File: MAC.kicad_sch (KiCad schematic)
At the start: 32 parts, among them J10 Conn_01x08_Male, U12 LM358, U13 LM358

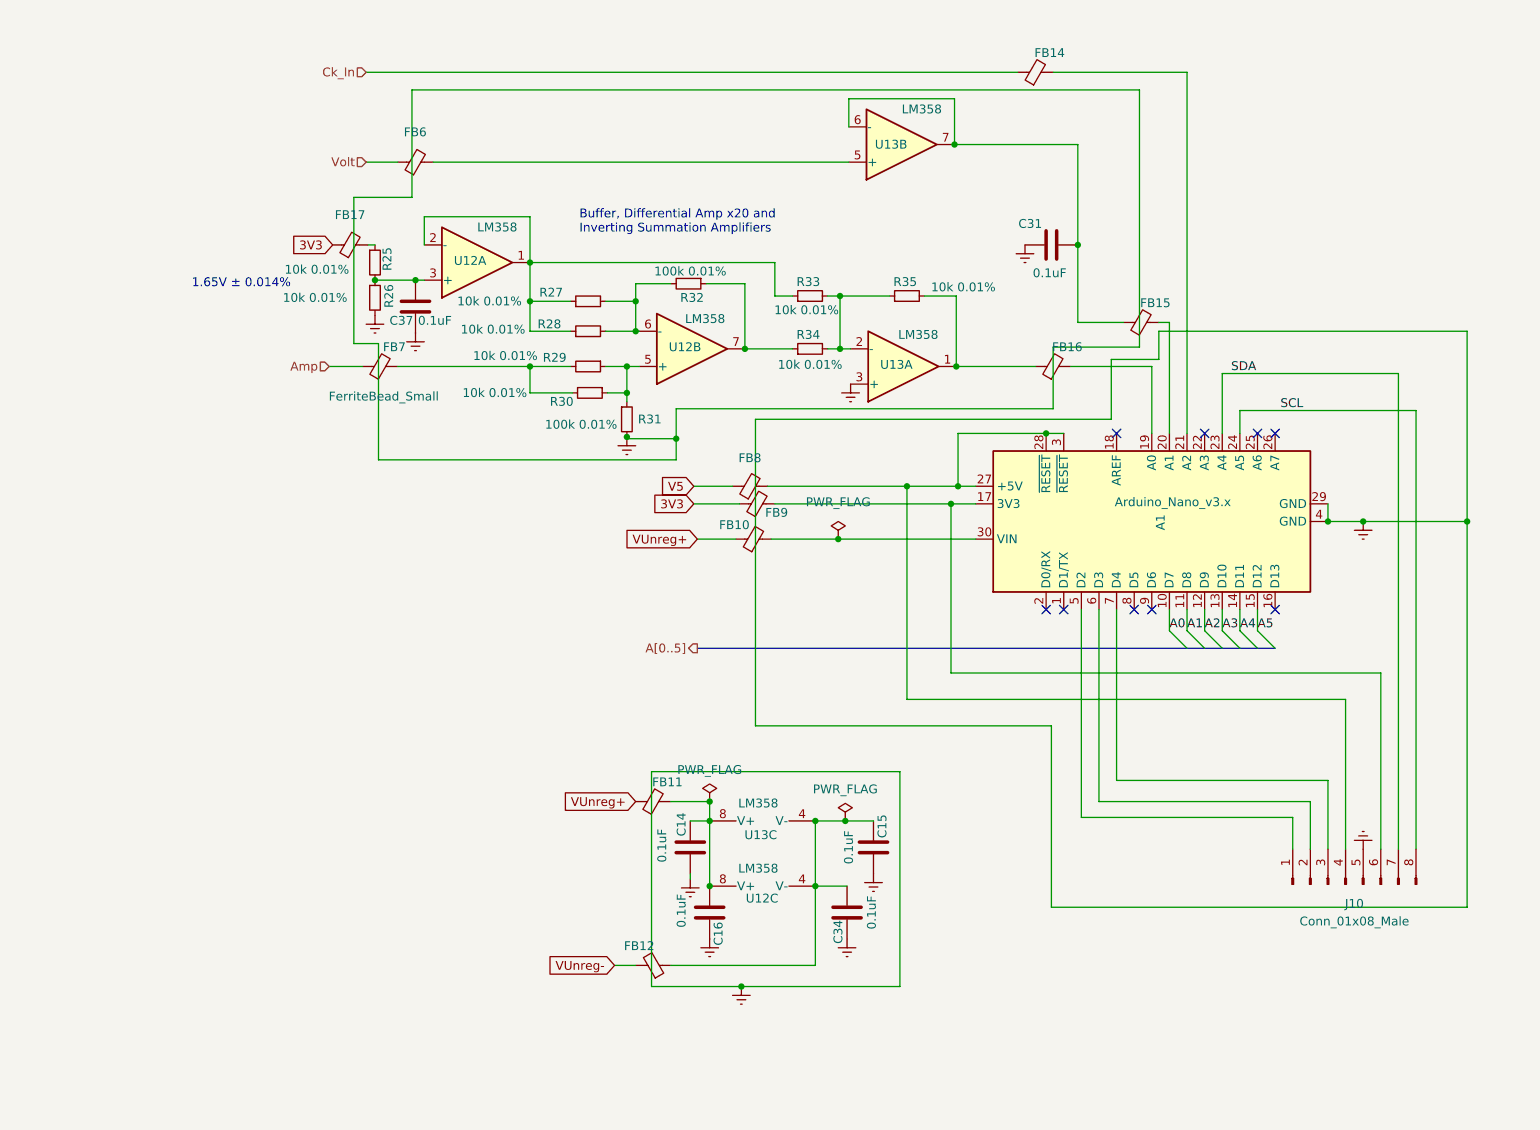
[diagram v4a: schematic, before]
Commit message: mux and opamp layouts completed and new ext conn to display
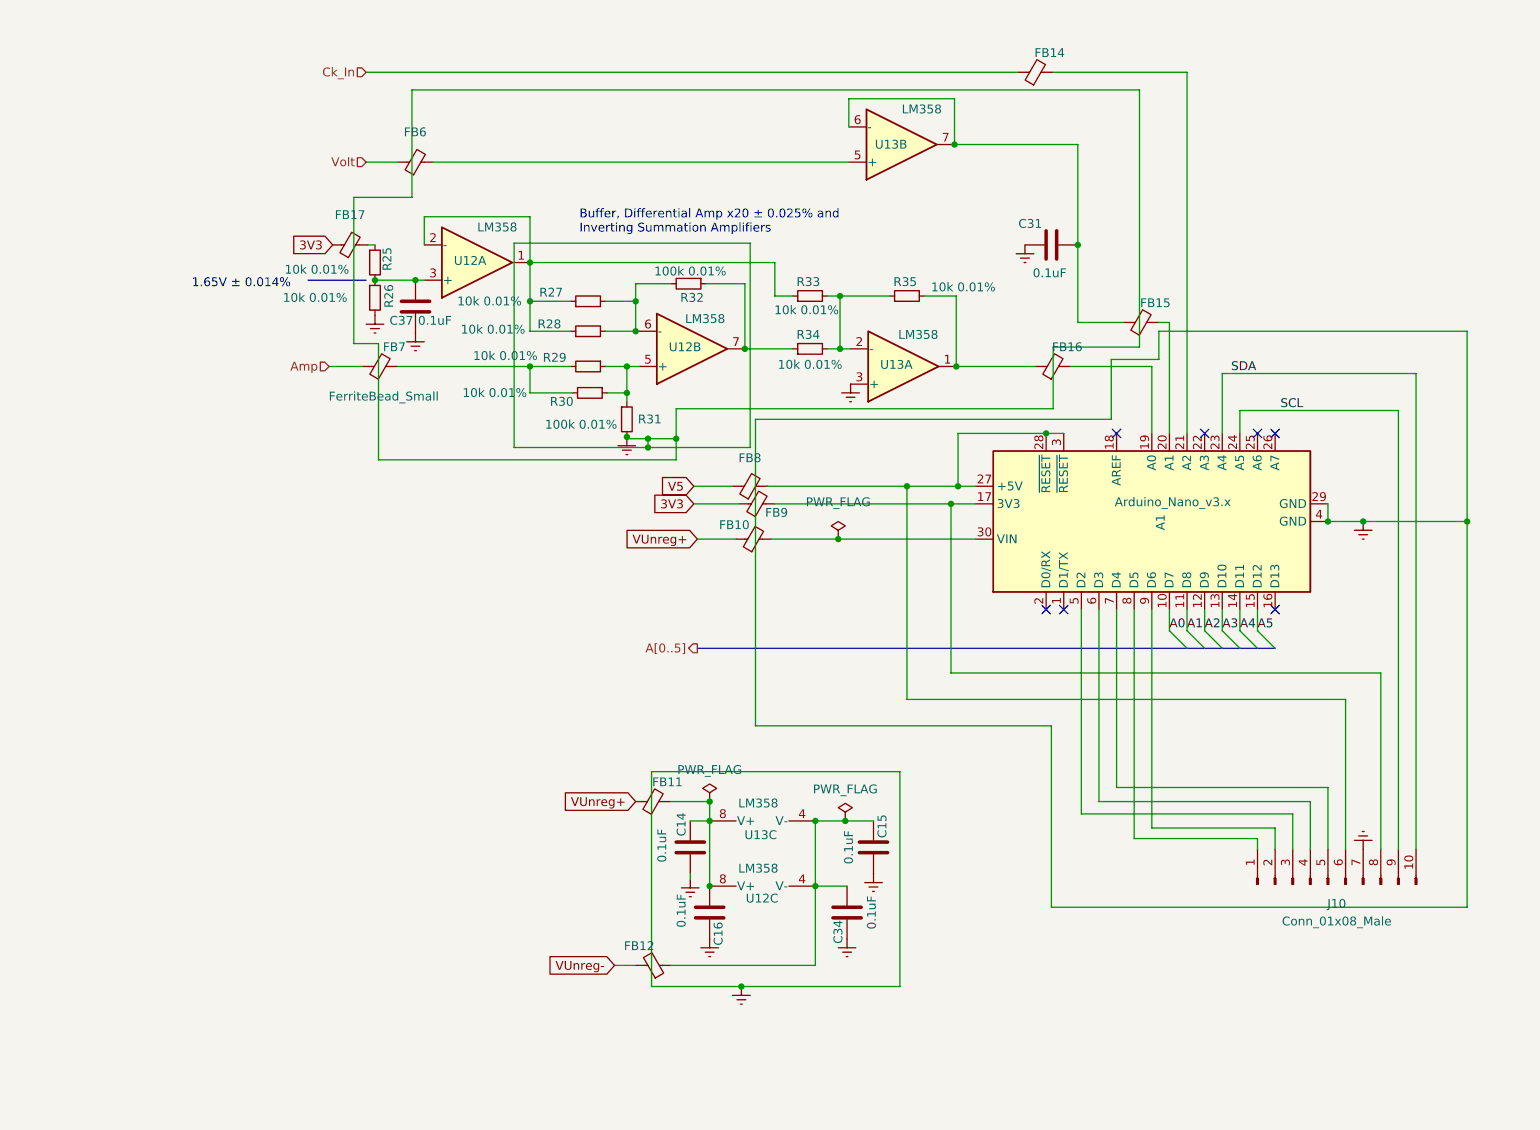
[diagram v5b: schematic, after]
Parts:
- J10: footprint Connector_PinHeader_2.54mm:PinHeader_1x08_P2.54mm_Vertical -> Connector_PinHeader_2.54mm:PinHeader_1x10_P2.54mm_Vertical; symbol Connector:Conn_01x08_Male -> Connector:Conn_01x10_Male
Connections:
- net GNDREF: now also J10.7 (Pin_7); no longer J10.5 (Pin_5)
- net SCL: now also J10.9 (Pin_9); no longer J10.8 (Pin_8)
- net SDA: now also J10.10 (Pin_10); no longer J10.7 (Pin_7)
- net at A1.17 (3V3), FB9.2: now also J10.8 (Pin_8); no longer J10.6 (Pin_6)
- net at J10.1 (Pin_1): now also A1.8 (D5); no longer A1.5 (D2)
- net at J10.2 (Pin_2): now also A1.9 (D6); no longer A1.6 (D3)
- net at J10.3 (Pin_3): now also A1.5 (D2); no longer A1.7 (D4)
- net at A1.27 (+5V), A1.28 (~{RESET}), A1.3 (~{RESET})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: now also J10.6 (Pin_6); no longer J10.4 (Pin_4)
- new net: A1.6 (D3), J10.4 (Pin_4)
- new net: A1.7 (D4), J10.5 (Pin_5)
- no-connect marks 9 -> 7
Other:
- note added: "Buffer, Differential Amp x20 ± 0.025% and Inverting Summation Amplifiers"
- note removed: "Buffer, Differential Amp x20 and Inverting Summation Amplifiers"
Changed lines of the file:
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@@
   (junction (at 120.142 138.684) (diameter 0) (color 0 0 0 0)
+  )
+  (junction (at 111.252 83.566) (diameter 0) (color 0 0 0 0)
+  )
+  (junction (at 111.252 84.836) (diameter 0) (color 0 0 0 0)
   )
   (junction (at 135.382 138.684) (diameter 0) (color 0 0 0 0)
@@
   (no_connect (at 171.196 108.204))
   (no_connect (at 168.656 108.204))
-  (no_connect (at 183.896 108.204))
-  (no_connect (at 181.356 108.204))
   (no_connect (at 201.676 82.804))
   (no_connect (at 191.516 82.804))
@@
     (stroke (width 0) (type default) (color 0 0 0 0))
   )
-  (wire (pts (xy 204.216 138.176) (xy 204.216 142.748))
+  (wire (pts (xy 204.216 137.668) (xy 204.216 142.748))
     (stroke (width 0) (type default) (color 0 0 0 0))
   )
@@
     (stroke (width 0) (type default) (color 0 0 0 0))
   )
+  (wire (pts (xy 91.948 55.372) (xy 91.948 84.836))
+    (stroke (width 0) (type default) (color 0 0 0 0))
+  )
   (wire (pts (xy 68.834 48.768) (xy 68.834 69.85))
     (stroke (width 0) (type default) (color 0 0 0 0))
@@
     (stroke (width 0) (type default) (color 0 0 0 0))
   )
+  (wire (pts (xy 181.356 141.224) (xy 199.136 141.224))
+    (stroke (width 0) (type default) (color 0 0 0 0))
+  )
+  (wire (pts (xy 181.356 108.204) (xy 181.356 141.224))
+    (stroke (width 0) (type default) (color 0 0 0 0))
+  )
   (wire (pts (xy 169.672 70.358) (xy 182.118 70.358))
     (stroke (width 0) (type default) (color 0 0 0 0))
@@
     (stroke (width 0) (type default) (color 0 0 0 0))
   )
+  (wire (pts (xy 91.948 55.372) (xy 125.984 55.372))
+    (stroke (width 0) (type default) (color 0 0 0 0))
+  )
   (wire (pts (xy 147.574 162.56) (xy 124.714 162.56))
     (stroke (width 0) (type default) (color 0 0 0 0))
@@
     (stroke (width 0) (type default) (color 0 0 0 0))
   )
+  (wire (pts (xy 201.676 142.748) (xy 201.676 139.7))
+    (stroke (width 0) (type default) (color 0 0 0 0))
+  )
   (wire (pts (xy 109.474 61.214) (xy 114.554 61.214))
     (stroke (width 0) (type default) (color 0 0 0 0))
@@
     (stroke (width 0) (type default) (color 0 0 0 0))
   )
+  (wire (pts (xy 219.456 79.502) (xy 219.456 142.748))
+    (stroke (width 0) (type default) (color 0 0 0 0))
+  )
   (wire (pts (xy 182.118 33.274) (xy 182.118 70.358))
     (stroke (width 0) (type default) (color 0 0 0 0))
   )
+  (wire (pts (xy 125.984 84.836) (xy 125.984 55.372))
+    (stroke (width 0) (type default) (color 0 0 0 0))
+  )
   (wire (pts (xy 68.834 48.768) (xy 77.216 48.768))
     (stroke (width 0) (type default) (color 0 0 0 0))
@@
     (stroke (width 0) (type default) (color 0 0 0 0))
   )
+  (wire (pts (xy 111.252 83.566) (xy 111.252 84.836))
+    (stroke (width 0) (type default) (color 0 0 0 0))
+  )
   (wire (pts (xy 77.724 60.706) (xy 78.994 60.706))
     (stroke (width 0) (type default) (color 0 0 0 0))
@@
     (stroke (width 0) (type default) (color 0 0 0 0))
   )
+  (wire (pts (xy 183.896 139.7) (xy 183.896 108.204))
+    (stroke (width 0) (type default) (color 0 0 0 0))
+  )
   (wire (pts (xy 115.316 86.614) (xy 115.316 83.566))
     (stroke (width 0) (type default) (color 0 0 0 0))
@@
     (stroke (width 0) (type default) (color 0 0 0 0))
   )
-  (wire (pts (xy 173.736 108.204) (xy 173.736 138.176))
+  (wire (pts (xy 173.736 108.204) (xy 173.736 137.668))
     (stroke (width 0) (type default) (color 0 0 0 0))
   )
@@
     (stroke (width 0) (type default) (color 0 0 0 0))
   )
-  (wire (pts (xy 196.596 79.502) (xy 221.996 79.502))
+  (wire (pts (xy 196.596 79.502) (xy 219.456 79.502))
     (stroke (width 0) (type default) (color 0 0 0 0))
   )
@@
     (stroke (width 0) (type default) (color 0 0 0 0))
   )
-  (wire (pts (xy 221.996 79.502) (xy 221.996 142.748))
-    (stroke (width 0) (type default) (color 0 0 0 0))
-  )
   (wire (pts (xy 117.856 92.964) (xy 124.46 92.964))
     (stroke (width 0) (type default) (color 0 0 0 0))
   )
-  (wire (pts (xy 173.736 138.176) (xy 204.216 138.176))
+  (wire (pts (xy 173.736 137.668) (xy 204.216 137.668))
     (stroke (width 0) (type default) (color 0 0 0 0))
   )
@@
     (stroke (width 0) (type default) (color 0 0 0 0))
   )
-  (wire (pts (xy 178.816 132.842) (xy 209.296 132.842))
+  (wire (pts (xy 178.816 133.858) (xy 209.296 133.858))
     (stroke (width 0) (type default) (color 0 0 0 0))
   )
@@
     (stroke (width 0) (type default) (color 0 0 0 0))
   )
+  (wire (pts (xy 91.948 84.836) (xy 111.252 84.836))
+    (stroke (width 0) (type default) (color 0 0 0 0))
+  )
   (wire (pts (xy 72.39 69.85) (xy 68.834 69.85))
     (stroke (width 0) (type default) (color 0 0 0 0))
@@
     (stroke (width 0) (type default) (color 0 0 0 0))
   )
-  (wire (pts (xy 108.204 83.566) (xy 115.316 83.566))
+  (wire (pts (xy 108.204 83.566) (xy 111.252 83.566))
     (stroke (width 0) (type default) (color 0 0 0 0))
   )
@@
     (stroke (width 0) (type default) (color 0 0 0 0))
   )
+  (wire (pts (xy 111.252 83.566) (xy 115.316 83.566))
+    (stroke (width 0) (type default) (color 0 0 0 0))
+  )
   (wire (pts (xy 140.208 34.544) (xy 155.448 34.544))
     (stroke (width 0) (type default) (color 0 0 0 0))
@@
     (stroke (width 0) (type default) (color 0 0 0 0))
   )
-  (wire (pts (xy 219.456 74.168) (xy 194.056 74.168))
+  (wire (pts (xy 201.676 139.7) (xy 183.896 139.7))
+    (stroke (width 0) (type default) (color 0 0 0 0))
+  )
+  (wire (pts (xy 194.056 74.168) (xy 221.996 74.168))
     (stroke (width 0) (type default) (color 0 0 0 0))
   )
@@
     (stroke (width 0) (type default) (color 0 0 0 0))
   )
+  (wire (pts (xy 221.996 74.168) (xy 221.996 142.748))
+    (stroke (width 0) (type default) (color 0 0 0 0))
+  )
   (wire (pts (xy 135.382 138.684) (xy 139.7 138.684))
     (stroke (width 0) (type default) (color 0 0 0 0))
@@
     (stroke (width 0) (type default) (color 0 0 0 0))
   )
-  (wire (pts (xy 219.456 74.168) (xy 219.456 142.748))
-    (stroke (width 0) (type default) (color 0 0 0 0))
-  )
   (wire (pts (xy 137.16 62.992) (xy 138.938 62.992))
     (stroke (width 0) (type default) (color 0 0 0 0))
@@
     (stroke (width 0) (type default) (color 0 0 0 0))
   )
-  (wire (pts (xy 178.816 108.204) (xy 178.816 132.842))
+  (wire (pts (xy 178.816 108.204) (xy 178.816 133.858))
     (stroke (width 0) (type default) (color 0 0 0 0))
   )
@@
     (stroke (width 0) (type default) (color 0 0 0 0))
   )
+  (wire (pts (xy 199.136 141.224) (xy 199.136 142.748))
+    (stroke (width 0) (type default) (color 0 0 0 0))
+  )
   (wire (pts (xy 120.142 135.89) (xy 120.142 138.684))
     (stroke (width 0) (type default) (color 0 0 0 0))
   )
+  (wire (pts (xy 111.252 84.836) (xy 125.984 84.836))
+    (stroke (width 0) (type default) (color 0 0 0 0))
+  )
   (bus (pts (xy 199.136 113.792) (xy 201.676 113.792))
     (stroke (width 0) (type default) (color 0 0 0 0))
@@
     (stroke (width 0) (type default) (color 0 0 0 0))
   )
+  (polyline (pts (xy 62.23 60.706) (xy 70.612 60.706))
+    (stroke (width 0) (type default) (color 0 0 0 0))
+  )
   (wire (pts (xy 129.54 58.166) (xy 94.234 58.166))
     (stroke (width 0) (type default) (color 0 0 0 0))
@@
     (stroke (width 0) (type default) (color 0 0 0 0))
   )
-  (wire (pts (xy 209.296 132.842) (xy 209.296 142.748))
+  (wire (pts (xy 209.296 133.858) (xy 209.296 142.748))
     (stroke (width 0) (type default) (color 0 0 0 0))
   )
@@
     (stroke (width 0) (type default) (color 0 0 0 0))
   )
-  (text "Buffer, Differential Amp x20 and\nInverting Summation Amplifiers"
+  (text "Buffer, Differential Amp x20 ± 0.025% and\nInverting Summation Amplifiers"
     (at 101.346 54.102 0)
     (effects (font (size 1.27 1.27)) (justify left bottom))
@@
     (pin "2")
   )
-  (symbol (lib_id "Connector:Conn_01x08_Male") (at 211.836 147.828 90) (unit 1)
+  (symbol (lib_id "Connector:Conn_01x10_Male") (at 209.296 147.828 90) (unit 1)
     (in_bom yes) (on_board yes) (fields_autoplaced)
-    (property "Reference" "J10" (id 0) (at 213.106 150.622 90))
-    (property "Value" "Conn_01x08_Male" (id 1) (at 213.106 153.162 90))
-    (property "Footprint" "Connector_PinHeader_2.54mm:PinHeader_1x08_P2.54mm_Vertical" (id 2) (at 211.836 147.828 0)
-      (effects (font (size 1.27 1.27)) hide)
-    )
-    (property "Datasheet" "~" (id 3) (at 211.836 147.828 0)
-      (effects (font (size 1.27 1.27)) hide)
-    )
-    (pin "1")
+    (property "Reference" "J10" (id 0) (at 210.566 150.622 90))
+    (property "Value" "Conn_01x08_Male" (id 1) (at 210.566 153.162 90))
+    (property "Footprint" "Connector_PinHeader_2.54mm:PinHeader_1x10_P2.54mm_Vertical" (id 2) (at 209.296 147.828 0)
+      (effects (font (size 1.27 1.27)) hide)
+    )
+    (property "Datasheet" "~" (id 3) (at 209.296 147.828 0)
+      (effects (font (size 1.27 1.27)) hide)
+    )
+    (pin "1")
+    (pin "10")
     (pin "2")
     (pin "3")
@@
     (pin "7")
     (pin "8")
+    (pin "9")
   )
   (symbol (lib_id "Device:FerriteBead_Small") (at 77.724 43.688 90) (unit 1)
